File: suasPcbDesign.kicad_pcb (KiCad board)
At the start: 4 copper layers, 71.6 x 100 mm, 99 parts, among them J1 SENSE_IB, J2 SPI CS, J4 SPI CTRL, J5 PWM CTRL, J6 JTAG Pinout, J7 USB_C_Receptacle_USB2.0_16P, M3x1 MountingHole_3.2mm_M3, M3x2 MountingHole_3.2mm_M3, M3x3 MountingHole_3.2mm_M3, M3x4 MountingHole_3.2mm_M3, SW1 SW_SPST, SW2 SW_SPST, SW3 SW_SPST, SW4 SW_SPST, SW5 SW_SPST, SW6 SW_SPST, SW7 SW_SPST, U1 74HC138, U2 LMR51625DDC, U3 MCP3562RT-E/ST, U4 MCP6486R, U5 TLV77733PDBVR, U6 LMV331, U7 ESP32-S3-WROOM-1, U8 LM66100DCK, U9 USBLC6-2SC6

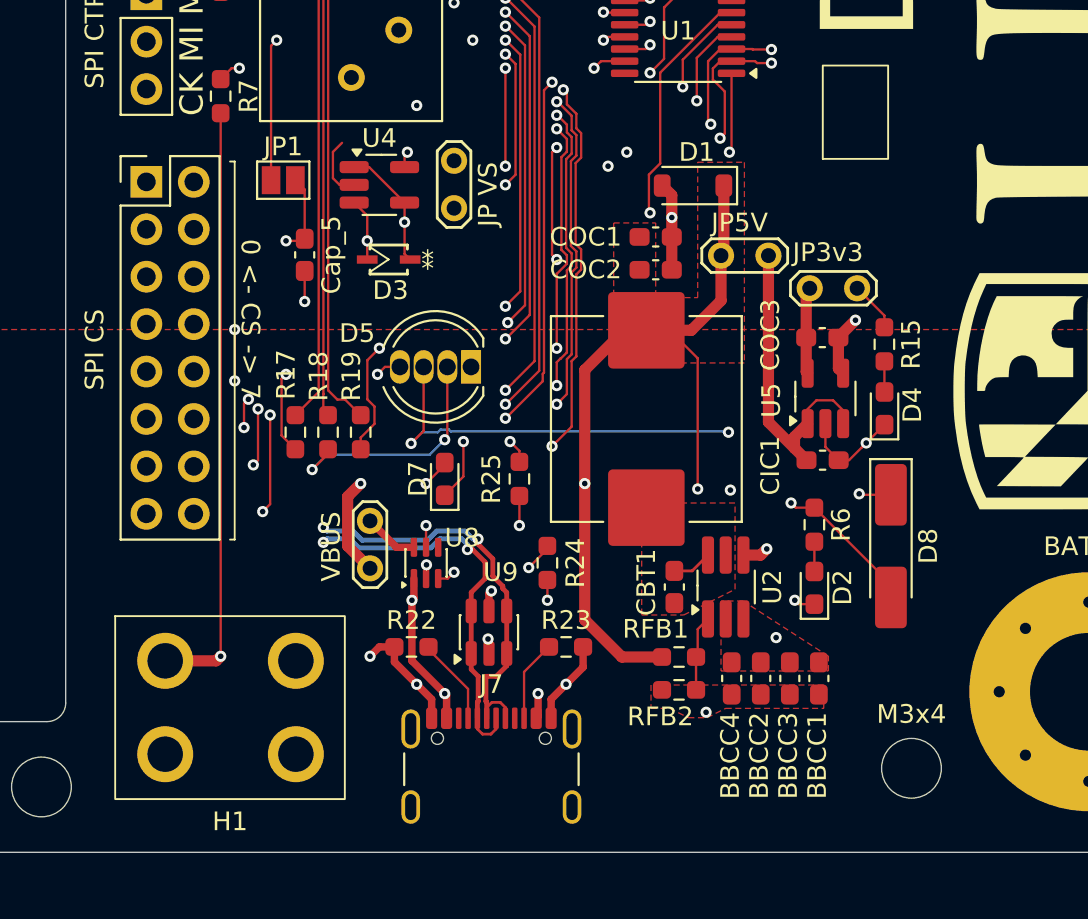
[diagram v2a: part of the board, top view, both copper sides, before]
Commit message: Add reverse polarity diode and edit resistor vals
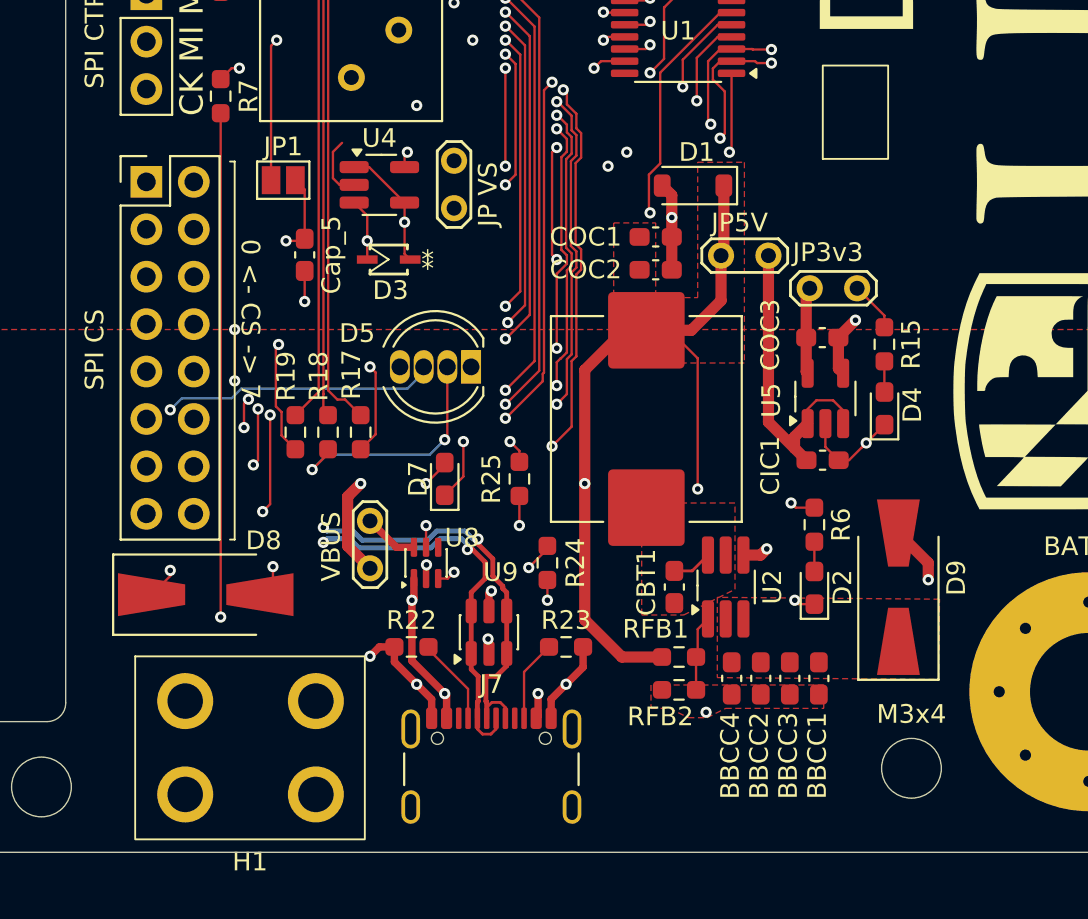
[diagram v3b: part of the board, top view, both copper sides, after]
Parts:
- added D9: D, Diode_SMD:D_SMA-SMB_Universal_Handsoldering, F.Cu at (131.3, 176.3)
- D8: footprint Diode_SMD:D_MiniMELF_Handsoldering -> Diode_SMD:D_SMA-SMB_Universal_Handsoldering
- R15: value 100R -> 200R
- R17, R18: value 62R -> 150R
- R19: value 110R -> 75R
- R6: value 200R -> 300R
- moved D8 36.8 mm to (94.2, 176.7), turned to 0 degrees
- moved R17 3.50 mm to (102.5, 168.0)
- moved R19 3.50 mm to (99.0, 168.0)
- moved H1 2.41 mm to (96.6, 184.9)
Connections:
- BBCC1 pad 1: /VIN -> Net-(D9-K)
- BBCC2 pad 1: /VIN -> Net-(D9-K)
- BBCC3 pad 1: /VIN -> Net-(D9-K)
- BBCC4 pad 1: /VIN -> Net-(D9-K)
- R17 pad 1: /IND_B -> /IND_R
- R19 pad 1: /IND_R -> /IND_B
- U2 pad 2: /VIN -> Net-(D9-K)
- U2 pad 3: /VIN -> Net-(D9-K)
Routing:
- net /VIN: track 63.4 -> 74.8 mm
- net Net-(D5-A): track 33.6 -> 25.0 mm, vias 4 -> 2
- net Net-(D5-BK): track 11.8 -> 17.1 mm
- net Net-(D5-RK): track 11.0 -> 6.47 mm, vias 2 -> 1
- net 5V: track 154.4 -> 154.9 mm, vias 10 -> 11
- added copper zone on F.Cu, net Net-(D9-K)
- removed copper zone on F.Cu, net /VIN
